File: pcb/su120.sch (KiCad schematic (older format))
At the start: 261 parts, among them J1 MJ-4PP-9, J2 Conn_01x03, J3 Conn_01x08, J4 Conn_01x08, J5 Conn_01x03, J6 MJ-4PP-9, SW1 SW_Push, SW10 SW_Push, SW11 SW_Push, SW12 SW_Push, SW13 SW_Push, SW14 SW_Push, SW15 SW_Push, SW16 SW_Push, SW17 SW_Push, SW18 SW_Push, SW19 SW_Push, SW2 SW_Push, SW20 SW_Push, SW3 SW_Push, SW4 SW_Push, SW5 SW_Push, SW6 SW_Push, SW7 SW_Push, SW8 SW_Push, SW9 SW_Push, U1 ProMicro

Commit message: Rev.3
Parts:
- removed H100, H101, H102, H103, H104, H105, H106, H107, H108, H109, H110, H111, H112, H141, H142, H143, H144, H145, H146, H147, H148, H149, H150, H151, H152, H49, H50, H51, H52, H53, H54, H55, H56, H57, H58, H59, H60, H61, H62, H63, H64, H65, H66, H67, H68, H69, H70, H71, H72, H73, H74, H75, H76, H77, H78, H79, H80, H81, H82, H83, H84, H85, H86, H87, H88, H89, H90, H91, H92, H93, H94, H95, H96, H97, H98, H99: MountingHole_Pad, #footprint:M2_Pad, symbol Mechanical:MountingHole_Pad
- removed H153, H154, H155, H156, H157, H158, H159, H160, H161, H162, H163, H164, H165, H166, H167, H168, H169, H170, H171, H172, H173, H174, H175, H176, H177, H178, H179, H180, H181, H182, H183, H184, H185, H186, H187, H188, H189, H190, H191, H192, H193, H194, H195, H196, H197, H198, H199, H200, H201, H202, H203, H204, H205, H206, H207, H208, H209: MountingHole_Pad, #footprint:M1.4_tapping_Pad, symbol Mechanical:MountingHole_Pad
- added D20: D, #footprint:diode_TH_SMD, symbol Device:D
- added H210, H211, H212, H213: MountingHole_Pad, #footprint:1pin_conn, symbol Mechanical:MountingHole_Pad
- added SW21: SW_Push, #footprint:CherryMX_MidHeight_Choc_Hotswap_rev4, symbol Switch:SW_Push
- SW1, SW10, SW11, SW12, SW13, SW14, SW15, SW16, SW17, SW19, SW2, SW20, SW3, SW4, SW5, SW6, SW7, SW8, SW9: footprint #footprint:CherryMX_MidHeight_Choc_Hotswap_rev2 -> #footprint:CherryMX_MidHeight_Choc_Hotswap_rev4
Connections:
- net X1: no longer H41.1, H43.1, SW16.1
- net X2: now also H41.1, H43.1, SW16.1
- net X5: now also H210.1, H211.1, SW21.1
- net Y5: now also D20.1 (K), H212.1, H213.1
- new net: D20.2 (A), SW21.2
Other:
- moved on the sheet: D16, H41, H43, H45, H46, SW16

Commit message: Rev.4
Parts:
- J3, J4: footprint #footprint:PinHeader_1x08_P2.54mm_Vertical -> #footprint:PinHeader_1x08_P2.54mm_Vertical_rev2
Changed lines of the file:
@@
 F 0 "J3" H 3980 3242 50  0000 L CNN
 F 1 "Conn_01x08" H 3980 3151 50  0000 L CNN
-F 2 "#footprint:PinHeader_1x08_P2.54mm_Vertical" H 3900 3250 50  0001 C CNN
+F 2 "#footprint:PinHeader_1x08_P2.54mm_Vertical_rev2" H 3900 3250 50  0001 C CNN
 F 3 "~" H 3900 3250 50  0001 C CNN
 	1    3900 3250
@@
 F 0 "J4" H 1670 3767 50  0000 C CNN
 F 1 "Conn_01x08" H 1670 3676 50  0000 C CNN
-F 2 "#footprint:PinHeader_1x08_P2.54mm_Vertical" H 1750 3250 50  0001 C CNN
+F 2 "#footprint:PinHeader_1x08_P2.54mm_Vertical_rev2" H 1750 3250 50  0001 C CNN
 F 3 "~" H 1750 3250 50  0001 C CNN
 	1    1750 3250

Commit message: fix PCB
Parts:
- SW1, SW10, SW11, SW12, SW13, SW14, SW15, SW16, SW17, SW19, SW2, SW20, SW21, SW3, SW4, SW5, SW6, SW7, SW8, SW9: footprint #footprint:CherryMX_MidHeight_Choc_Hotswap_rev4 -> #footprint:CherryMX_Choc_Hotswap_rev4
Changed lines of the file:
@@
 encoding utf-8
 Sheet 1 1
-Title "SU120 (Yakitori Keyboard)"
+Title "SU120 Yakitori Keyboard"
 Date ""
-Rev "3"
+Rev "4"
 Comp "@e3w2q"
 Comment1 ""
@@
 F 0 "SW1" H 6200 2085 50  0000 C CNN
 F 1 "SW_Push" H 6200 1994 50  0000 C CNN
-F 2 "#footprint:CherryMX_MidHeight_Choc_Hotswap_rev4" H 6200 2000 50  0001 C CNN
+F 2 "#footprint:CherryMX_Choc_Hotswap_rev4" H 6200 2000 50  0001 C CNN
 F 3 "" H 6200 2000 50  0001 C CNN
 	1    6200 1800
@@
 F 0 "SW2" H 7250 2085 50  0000 C CNN
 F 1 "SW_Push" H 7250 1994 50  0000 C CNN
-F 2 "#footprint:CherryMX_MidHeight_Choc_Hotswap_rev4" H 7250 2000 50  0001 C CNN
+F 2 "#footprint:CherryMX_Choc_Hotswap_rev4" H 7250 2000 50  0001 C CNN
 F 3 "" H 7250 2000 50  0001 C CNN
 	1    7250 1800
@@
 F 0 "SW3" H 8350 2085 50  0000 C CNN
 F 1 "SW_Push" H 8350 1994 50  0000 C CNN
-F 2 "#footprint:CherryMX_MidHeight_Choc_Hotswap_rev4" H 8350 2000 50  0001 C CNN
+F 2 "#footprint:CherryMX_Choc_Hotswap_rev4" H 8350 2000 50  0001 C CNN
 F 3 "" H 8350 2000 50  0001 C CNN
 	1    8350 1800
@@
 F 0 "SW4" H 9400 2085 50  0000 C CNN
 F 1 "SW_Push" H 9400 1994 50  0000 C CNN
-F 2 "#footprint:CherryMX_MidHeight_Choc_Hotswap_rev4" H 9400 2000 50  0001 C CNN
+F 2 "#footprint:CherryMX_Choc_Hotswap_rev4" H 9400 2000 50  0001 C CNN
 F 3 "" H 9400 2000 50  0001 C CNN
 	1    9400 1800
@@
 F 0 "SW6" H 6200 2685 50  0000 C CNN
 F 1 "SW_Push" H 6200 2594 50  0000 C CNN
-F 2 "#footprint:CherryMX_MidHeight_Choc_Hotswap_rev4" H 6200 2600 50  0001 C CNN
+F 2 "#footprint:CherryMX_Choc_Hotswap_rev4" H 6200 2600 50  0001 C CNN
 F 3 "" H 6200 2600 50  0001 C CNN
 	1    6200 2400
@@
 F 0 "SW7" H 7250 2685 50  0000 C CNN
 F 1 "SW_Push" H 7250 2594 50  0000 C CNN
-F 2 "#footprint:CherryMX_MidHeight_Choc_Hotswap_rev4" H 7250 2600 50  0001 C CNN
+F 2 "#footprint:CherryMX_Choc_Hotswap_rev4" H 7250 2600 50  0001 C CNN
 F 3 "" H 7250 2600 50  0001 C CNN
 	1    7250 2400
@@
 F 0 "SW8" H 8350 2685 50  0000 C CNN
 F 1 "SW_Push" H 8350 2594 50  0000 C CNN
-F 2 "#footprint:CherryMX_MidHeight_Choc_Hotswap_rev4" H 8350 2600 50  0001 C CNN
+F 2 "#footprint:CherryMX_Choc_Hotswap_rev4" H 8350 2600 50  0001 C CNN
 F 3 "" H 8350 2600 50  0001 C CNN
 	1    8350 2400
@@
 F 0 "SW9" H 9400 2685 50  0000 C CNN
 F 1 "SW_Push" H 9400 2594 50  0000 C CNN
-F 2 "#footprint:CherryMX_MidHeight_Choc_Hotswap_rev4" H 9400 2600 50  0001 C CNN
+F 2 "#footprint:CherryMX_Choc_Hotswap_rev4" H 9400 2600 50  0001 C CNN
 F 3 "" H 9400 2600 50  0001 C CNN
 	1    9400 2400
@@
 F 0 "SW5" H 10450 2085 50  0000 C CNN
 F 1 "SW_Push" H 10450 1994 50  0000 C CNN
-F 2 "#footprint:CherryMX_MidHeight_Choc_Hotswap_rev4" H 10450 2000 50  0001 C CNN
+F 2 "#footprint:CherryMX_Choc_Hotswap_rev4" H 10450 2000 50  0001 C CNN
 F 3 "" H 10450 2000 50  0001 C CNN
 	1    10450 1800
@@
 F 0 "SW10" H 10450 2685 50  0000 C CNN
 F 1 "SW_Push" H 10450 2594 50  0000 C CNN
-F 2 "#footprint:CherryMX_MidHeight_Choc_Hotswap_rev4" H 10450 2600 50  0001 C CNN
+F 2 "#footprint:CherryMX_Choc_Hotswap_rev4" H 10450 2600 50  0001 C CNN
 F 3 "" H 10450 2600 50  0001 C CNN
 	1    10450 2400
@@
 F 0 "SW16" H 7250 3885 50  0000 C CNN
 F 1 "SW_Push" H 7250 3794 50  0000 C CNN
-F 2 "#footprint:CherryMX_MidHeight_Choc_Hotswap_rev4" H 7250 3800 50  0001 C CNN
+F 2 "#footprint:CherryMX_Choc_Hotswap_rev4" H 7250 3800 50  0001 C CNN
 F 3 "" H 7250 3800 50  0001 C CNN
 	1    7250 3600
@@
 F 0 "SW17" H 9400 3885 50  0000 C CNN
 F 1 "SW_Push" H 9400 3794 50  0000 C CNN
-F 2 "#footprint:CherryMX_MidHeight_Choc_Hotswap_rev4" H 9400 3800 50  0001 C CNN
+F 2 "#footprint:CherryMX_Choc_Hotswap_rev4" H 9400 3800 50  0001 C CNN
 F 3 "" H 9400 3800 50  0001 C CNN
 	1    9400 3600
@@
 F 0 "SW11" H 6200 3285 50  0000 C CNN
 F 1 "SW_Push" H 6200 3194 50  0000 C CNN
-F 2 "#footprint:CherryMX_MidHeight_Choc_Hotswap_rev4" H 6200 3200 50  0001 C CNN
+F 2 "#footprint:CherryMX_Choc_Hotswap_rev4" H 6200 3200 50  0001 C CNN
 F 3 "" H 6200 3200 50  0001 C CNN
 	1    6200 3000
@@
 F 0 "SW12" H 7250 3285 50  0000 C CNN
 F 1 "SW_Push" H 7250 3194 50  0000 C CNN
-F 2 "#footprint:CherryMX_MidHeight_Choc_Hotswap_rev4" H 7250 3200 50  0001 C CNN
+F 2 "#footprint:CherryMX_Choc_Hotswap_rev4" H 7250 3200 50  0001 C CNN
 F 3 "" H 7250 3200 50  0001 C CNN
 	1    7250 3000
@@
 F 0 "SW13" H 8350 3285 50  0000 C CNN
 F 1 "SW_Push" H 8350 3194 50  0000 C CNN
-F 2 "#footprint:CherryMX_MidHeight_Choc_Hotswap_rev4" H 8350 3200 50  0001 C CNN
+F 2 "#footprint:CherryMX_Choc_Hotswap_rev4" H 8350 3200 50  0001 C CNN
 F 3 "" H 8350 3200 50  0001 C CNN
 	1    8350 3000
@@
 F 0 "SW14" H 9400 3285 50  0000 C CNN
 F 1 "SW_Push" H 9400 3194 50  0000 C CNN
-F 2 "#footprint:CherryMX_MidHeight_Choc_Hotswap_rev4" H 9400 3200 50  0001 C CNN
+F 2 "#footprint:CherryMX_Choc_Hotswap_rev4" H 9400 3200 50  0001 C CNN
 F 3 "" H 9400 3200 50  0001 C CNN
 	1    9400 3000
@@
 F 0 "SW15" H 10450 3285 50  0000 C CNN
 F 1 "SW_Push" H 10450 3194 50  0000 C CNN
-F 2 "#footprint:CherryMX_MidHeight_Choc_Hotswap_rev4" H 10450 3200 50  0001 C CNN
+F 2 "#footprint:CherryMX_Choc_Hotswap_rev4" H 10450 3200 50  0001 C CNN
 F 3 "" H 10450 3200 50  0001 C CNN
 	1    10450 3000
@@
 F 0 "SW19" H 9400 1485 50  0000 C CNN
 F 1 "SW_Push" H 9400 1394 50  0000 C CNN
-F 2 "#footprint:CherryMX_MidHeight_Choc_Hotswap_rev4" H 9400 1400 50  0001 C CNN
+F 2 "#footprint:CherryMX_Choc_Hotswap_rev4" H 9400 1400 50  0001 C CNN
 F 3 "" H 9400 1400 50  0001 C CNN
 	1    9400 1200
@@
 F 0 "SW20" H 10450 1485 50  0000 C CNN
 F 1 "SW_Push" H 10450 1394 50  0000 C CNN
-F 2 "#footprint:CherryMX_MidHeight_Choc_Hotswap_rev4" H 10450 1400 50  0001 C CNN
+F 2 "#footprint:CherryMX_Choc_Hotswap_rev4" H 10450 1400 50  0001 C CNN
 F 3 "" H 10450 1400 50  0001 C CNN
 	1    10450 1200
@@
 F 0 "SW21" H 10450 3885 50  0000 C CNN
 F 1 "SW_Push" H 10450 3794 50  0000 C CNN
-F 2 "#footprint:CherryMX_MidHeight_Choc_Hotswap_rev4" H 10450 3800 50  0001 C CNN
+F 2 "#footprint:CherryMX_Choc_Hotswap_rev4" H 10450 3800 50  0001 C CNN
 F 3 "" H 10450 3800 50  0001 C CNN
 	1    10450 3600

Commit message: rev5
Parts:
- added H49, H50: MountingHole_Pad, #footprint:1pin_conn, symbol Mechanical:MountingHole_Pad
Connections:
- net Y5: now also H49.1, H50.1
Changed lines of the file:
@@
 Title "SU120 Yakitori Keyboard"
 Date ""
-Rev "4"
+Rev "5"
 Comp "@e3w2q"
 Comment1 ""
@@
 Connection ~ 10250 3150
 Wire Wire Line
-	7650 3900 9400 3900
-Wire Wire Line
-	5600 3900 7250 3900
+	7650 3900 7750 3900
+Wire Wire Line
+	5600 3900 7150 3900
 Wire Wire Line
 	5600 3300 6200 3300
@@
 Wire Wire Line
 	6000 800  6000 1650
+$Comp
+L Mechanical:MountingHole_Pad H50
+U 1 1 5D363A98
+P 7750 3800
+F 0 "H50" H 7850 3851 50  0000 L CNN
+F 1 "MountingHole_Pad" H 7850 3760 50  0000 L CNN
+F 2 "#footprint:1pin_conn" H 7750 3800 50  0001 C CNN
+F 3 "~" H 7750 3800 50  0001 C CNN
+	1    7750 3800
+	1    0    0    -1
+$EndComp
+Connection ~ 7750 3900
+Wire Wire Line
+	7750 3900 9400 3900
+$Comp
+L Mechanical:MountingHole_Pad H49
+U 1 1 5D363BD2
+P 7150 3800
+F 0 "H49" H 7250 3851 50  0000 L CNN
+F 1 "MountingHole_Pad" H 7250 3760 50  0000 L CNN
+F 2 "#footprint:1pin_conn" H 7150 3800 50  0001 C CNN
+F 3 "~" H 7150 3800 50  0001 C CNN
+	1    7150 3800
+	1    0    0    -1
+$EndComp
+Connection ~ 7150 3900
+Wire Wire Line
+	7150 3900 7250 3900
 $EndSCHEMATC

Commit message: Rev6
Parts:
- removed SW19, SW20: SW_Push, #footprint:CherryMX_Choc_Hotswap_rev4, symbol Switch:SW_Push
- added H51, H52, H53, H54, H55, H56: MountingHole_Pad, #footprint:1pin_conn, symbol Mechanical:MountingHole_Pad
- added SW19, SW20: Rotary_Encoder_Switch, #footprint:RotaryEncoder_Alps_EC11E-Switch_Vertical_H20mm_rev2, symbol Device:Rotary_Encoder_Switch
- SW1, SW10, SW11, SW12, SW13, SW14, SW15, SW16, SW17, SW2, SW3, SW4, SW5, SW6, SW7, SW8, SW9: footprint #footprint:CherryMX_Choc_Hotswap_rev4 -> #footprint:CherryMX_MidHeight_Choc_Hotswap_rev5
- U1: footprint #footprint:ArduinoProMicro-ZigZag_rev4 -> #footprint:ArduinoProMicro-ZigZag_rev5
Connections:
- net GND: now also H52.1, H55.1, SW19.C, SW20.C
- net X10: now also H56.1, SW20.B
- net X4: now also SW19.S1
- net X5: now also SW20.S1
- net X7: now also H51.1, SW19.A
- net X8: now also H53.1, SW19.B
- net X9: now also H54.1, SW20.A
- net Y1: now also D1.1 (K), D2.1 (K), D3.1 (K), D4.1 (K), D5.1 (K), H11.1, H12.1, H13.1, H14.1, H15.1, H16.1, H17.1, H18.1, H19.1, H20.1; no longer D18.1 (K), D19.1 (K), H137.1, H138.1, H139.1, H140.1
- net Y2: now also D10.1 (K), D6.1 (K), D7.1 (K), D8.1 (K), D9.1 (K), H31.1, H32.1, H33.1, H34.1, H35.1, H36.1, H37.1, H38.1, H39.1, H40.1; no longer D1.1 (K), D2.1 (K), D3.1 (K), D4.1 (K), D5.1 (K), H11.1, H12.1, H13.1, H14.1, H15.1, H16.1, H17.1, H18.1, H19.1, H20.1
- net Y3: now also D11.1 (K), D12.1 (K), D13.1 (K), D14.1 (K), D15.1 (K), H123.1, H124.1, H125.1, H126.1, H127.1, H128.1, H129.1, H130.1, H131.1, H132.1; no longer D10.1 (K), D6.1 (K), D7.1 (K), D8.1 (K), D9.1 (K), H31.1, H32.1, H33.1, H34.1, H35.1, H36.1, H37.1, H38.1, H39.1, H40.1
- net Y4: now also D16.1 (K), D17.1 (K), D20.1 (K), H212.1, H213.1, H45.1, H46.1, H47.1, H48.1, H49.1, H50.1; no longer D11.1 (K), D12.1 (K), D13.1 (K), D14.1 (K), D15.1 (K), H123.1, H124.1, H125.1, H126.1, H127.1, H128.1, H129.1, H130.1, H131.1, H132.1
- net Y5: no longer D16.1 (K), D17.1 (K), D20.1 (K), H212.1, H213.1, H45.1, H46.1, H47.1, H48.1, H49.1, H50.1
- net Y6: now also D18.1 (K), D19.1 (K), H137.1, H138.1, H139.1, H140.1
- net at D18.2 (A): now also SW19.S2
- net at D19.2 (A): now also SW20.S2
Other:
- moved on the sheet: D18, D19, H133, H134, H135, H136, H137, H138, H139, H140, SW18

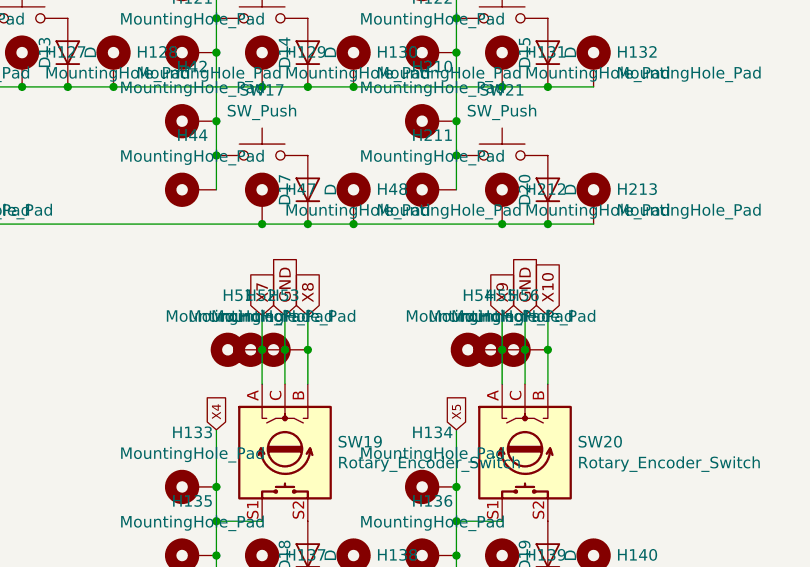
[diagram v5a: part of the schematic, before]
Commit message: Rotary Encoder's pin exchanged
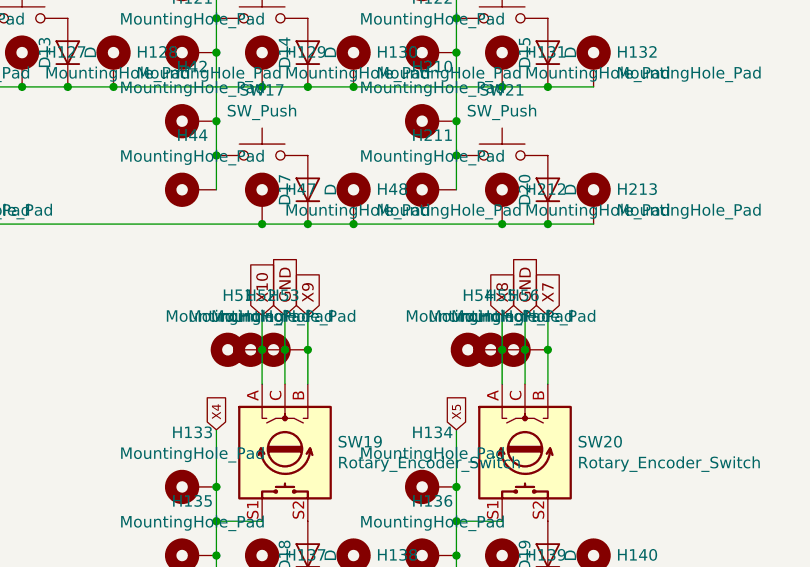
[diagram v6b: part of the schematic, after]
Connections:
- net X10: now also H51.1, SW19.A; no longer H56.1, SW20.B
- net X7: now also H56.1, SW20.B; no longer H51.1, SW19.A
- net X8: now also H54.1, SW20.A; no longer H53.1, SW19.B
- net X9: now also H53.1, SW19.B; no longer H54.1, SW20.A
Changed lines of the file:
@@
 	9200 800  9200 1650
 Connection ~ 9200 1650
+Text GLabel 10650 4300 1    50   Input ~ 0
+X7
+Text GLabel 10450 4300 1    50   Input ~ 0
+X8
+Text GLabel 9600 4300 1    50   Input ~ 0
+X9
 Text GLabel 9400 4300 1    50   Input ~ 0
-X7
-Text GLabel 9600 4300 1    50   Input ~ 0
-X8
-Text GLabel 10450 4300 1    50   Input ~ 0
-X9
-Text GLabel 10650 4300 1    50   Input ~ 0
 X10
 $Comp
